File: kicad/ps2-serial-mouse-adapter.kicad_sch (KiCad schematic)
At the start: 12 parts, among them U1 Arduino_Mini, U2 MAX232

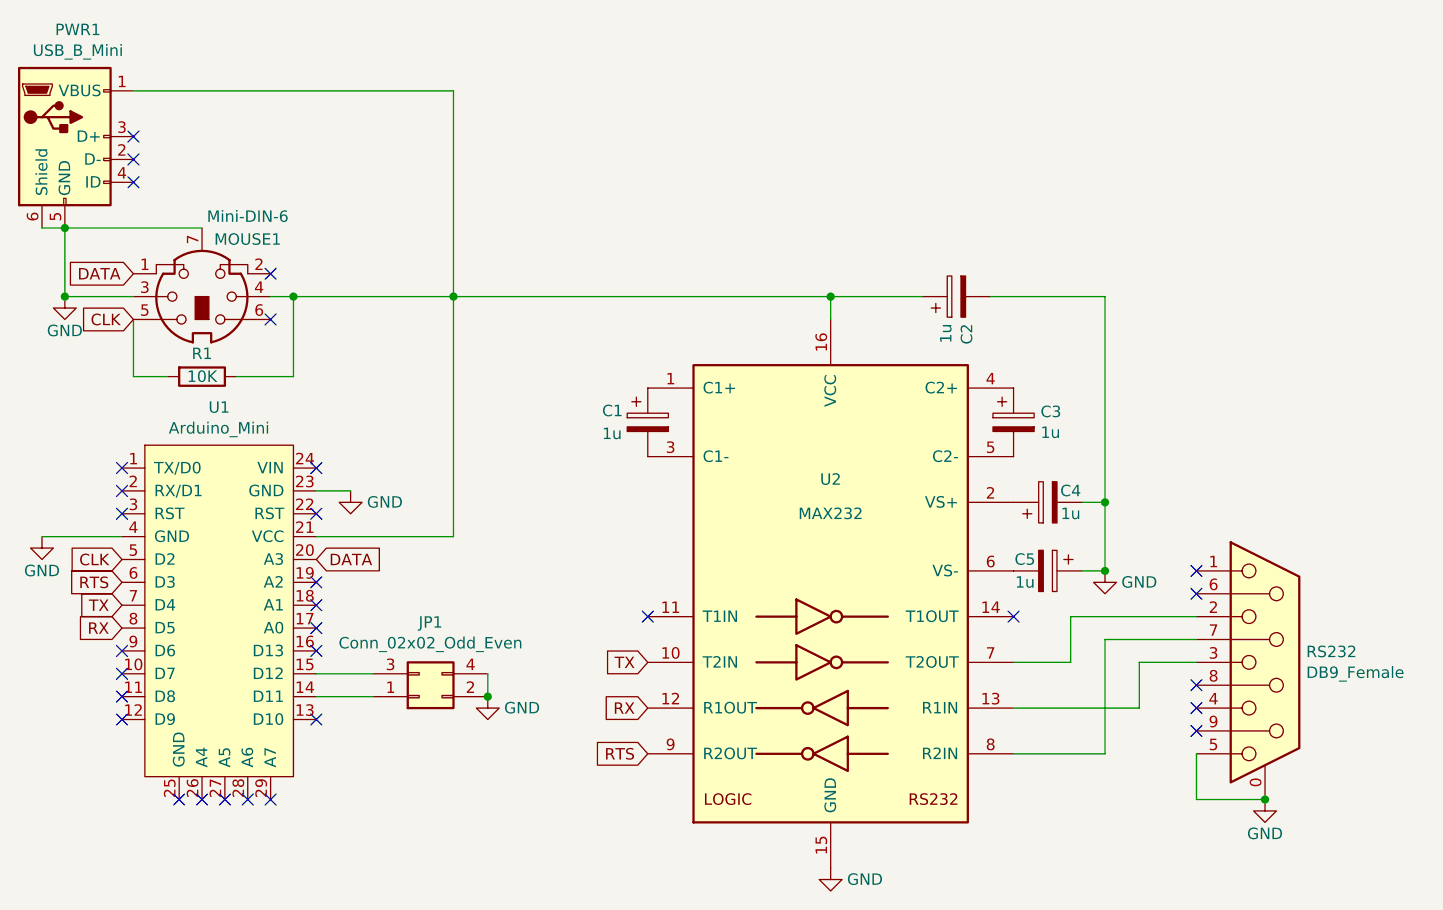
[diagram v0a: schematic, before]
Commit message: Switched charge pump from GND to VCC
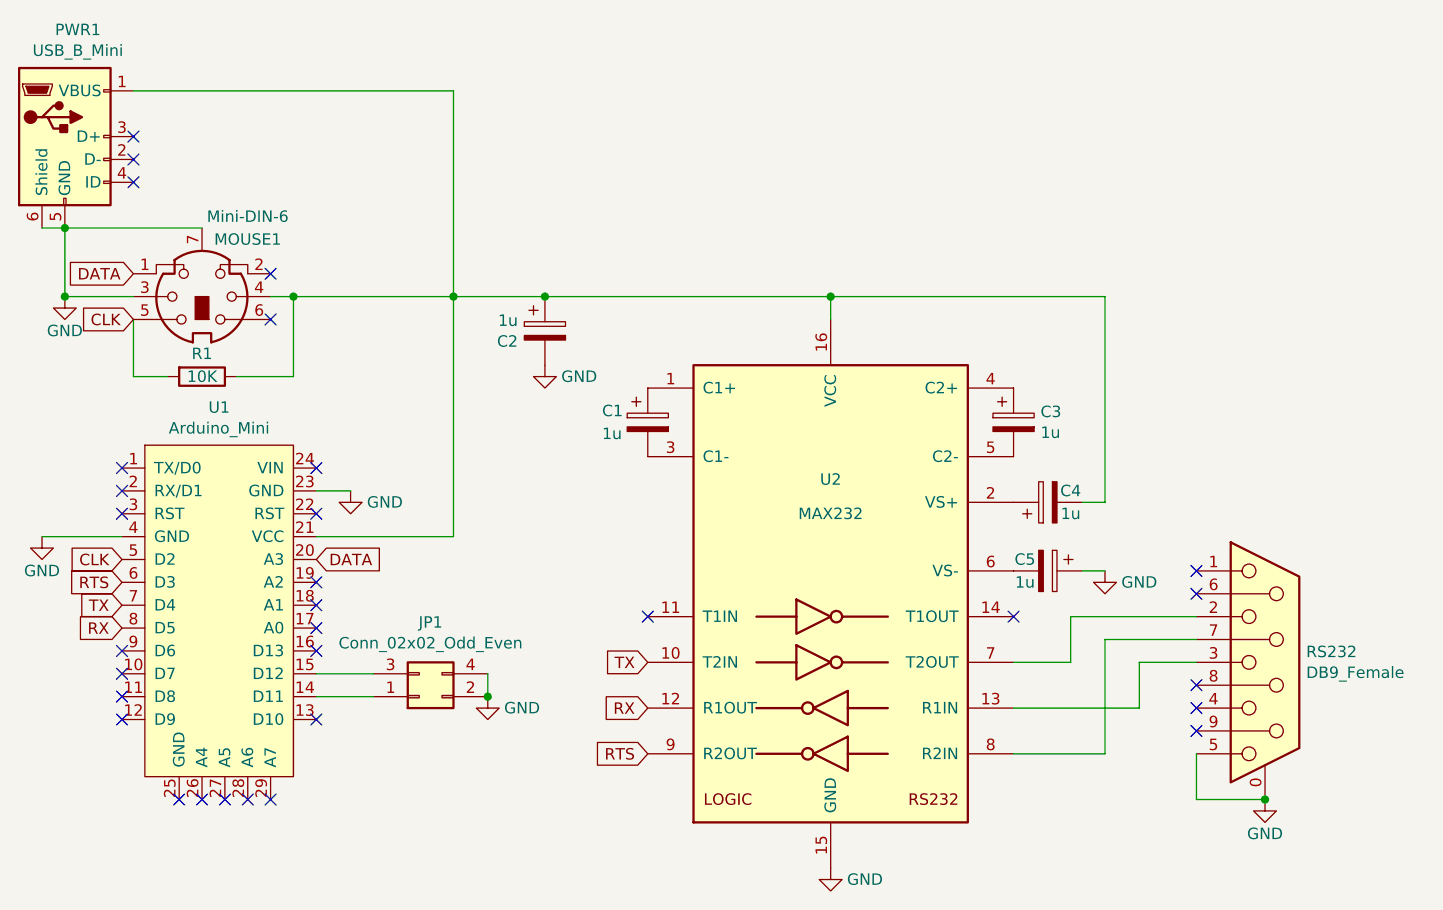
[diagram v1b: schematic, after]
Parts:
- MOUSE1: footprint Necroware:Mini_DIN_6_LCSC_C77848 -> ps2-serial-mouse-adapter:Mini_DIN_6_LCSC_C77848
- PWR1: footprint MyLibrary:USB_Mini-B-Jing_Extension_LSCS_C46398 -> ps2-serial-mouse-adapter:USB_Mini-B-Jing_Extension_LSCS_C46398
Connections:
- net GND: no longer C4.2
- net at C2.1, MOUSE1.4, PWR1.1 (VBUS)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: now also C4.2
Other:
- moved on the sheet: C2
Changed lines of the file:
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@@
   (title_block
     (title "PS/2 to Serial Mouse Adapter")
-    (date "2021-10-22")
-    (rev "0.7")
+    (date "2023-01-22")
+    (rev "0.8")
     (company "Necroware")
     (comment 1 "by Scorp")
@@
   (junction (at 100.33 60.96) (diameter 0) (color 0 0 0 0)
   )
+  (junction (at 160.02 60.96) (diameter 0) (color 0 0 0 0)
+  )
   (junction (at 74.93 60.96) (diameter 0) (color 0 0 0 0)
   )
@@
   (junction (at 118.11 60.96) (diameter 0) (color 0 0 0 0)
   )
-  (junction (at 160.02 60.96) (diameter 0) (color 0 0 0 0)
-  )
   (junction (at 121.92 105.41) (diameter 0) (color 0 0 0 0)
   )
-  (junction (at 190.5 83.82) (diameter 0) (color 0 0 0 0)
-  )
-  (junction (at 190.5 91.44) (diameter 0) (color 0 0 0 0)
+  (junction (at 128.27 60.96) (diameter 0) (color 0 0 0 0)
   )
   (no_connect (at 102.87 97.79))
@@
     (stroke (width 0) (type default) (color 0 0 0 0))
   )
-  (wire (pts (xy 177.8 60.96) (xy 190.5 60.96))
+  (wire (pts (xy 160.02 60.96) (xy 190.5 60.96))
     (stroke (width 0) (type default) (color 0 0 0 0))
   )
@@
     (stroke (width 0) (type default) (color 0 0 0 0))
   )
-  (wire (pts (xy 170.18 60.96) (xy 160.02 60.96))
-    (stroke (width 0) (type default) (color 0 0 0 0))
-  )
   (wire (pts (xy 118.11 87.63) (xy 118.11 60.96))
     (stroke (width 0) (type default) (color 0 0 0 0))
   )
-  (wire (pts (xy 118.11 60.96) (xy 160.02 60.96))
+  (wire (pts (xy 118.11 60.96) (xy 128.27 60.96))
     (stroke (width 0) (type default) (color 0 0 0 0))
   )
@@
     (stroke (width 0) (type default) (color 0 0 0 0))
   )
-  (wire (pts (xy 190.5 83.82) (xy 190.5 91.44))
+  (wire (pts (xy 128.27 60.96) (xy 160.02 60.96))
     (stroke (width 0) (type default) (color 0 0 0 0))
   )
@@
     (property "Reference" "MOUSE1" (id 0) (at 95.25 54.61 0))
     (property "Value" "Mini-DIN-6" (id 1) (at 95.25 52.07 0))
-    (property "Footprint" "Necroware:Mini_DIN_6_LCSC_C77848" (id 2) (at 90.17 60.96 0)
+    (property "Footprint" "ps2-serial-mouse-adapter:Mini_DIN_6_LCSC_C77848" (id 2) (at 90.17 60.96 0)
       (effects (font (size 1.27 1.27)) hide)
     )
@@
     (pin "2")
   )
-  (symbol (lib_id "ps2-serial-mouse-adapter-rescue:CP-Device") (at 173.99 60.96 90) (unit 1)
-    (in_bom yes) (on_board yes)
-    (property "Reference" "C2" (id 0) (at 175.1584 63.9572 0)
+  (symbol (lib_id "ps2-serial-mouse-adapter-rescue:CP-Device") (at 128.27 64.77 0) (unit 1)
+    (in_bom yes) (on_board yes)
+    (property "Reference" "C2" (id 0) (at 125.2728 65.9384 0)
       (effects (font (size 1.27 1.27)) (justify right))
     )
-    (property "Value" "1u" (id 1) (at 172.847 63.9572 0)
+    (property "Value" "1u" (id 1) (at 125.2728 63.627 0)
       (effects (font (size 1.27 1.27)) (justify right))
     )
-    (property "Footprint" "Capacitor_THT:CP_Radial_D4.0mm_P1.50mm" (id 2) (at 177.8 59.9948 0)
-      (effects (font (size 1.27 1.27)) hide)
-    )
-    (property "Datasheet" "~" (id 3) (at 173.99 60.96 0)
+    (property "Footprint" "Capacitor_THT:CP_Radial_D4.0mm_P1.50mm" (id 2) (at 129.2352 68.58 0)
+      (effects (font (size 1.27 1.27)) hide)
+    )
+    (property "Datasheet" "~" (id 3) (at 128.27 64.77 0)
       (effects (font (size 1.27 1.27)) hide)
     )
@@
     (property "Reference" "PWR1" (id 0) (at 76.3778 31.3182 0))
     (property "Value" "USB_B_Mini" (id 1) (at 76.3778 33.6296 0))
-    (property "Footprint" "MyLibrary:USB_Mini-B-Jing_Extension_LSCS_C46398" (id 2) (at 78.74 44.45 0)
+    (property "Footprint" "ps2-serial-mouse-adapter:USB_Mini-B-Jing_Extension_LSCS_C46398" (id 2) (at 78.74 44.45 0)
       (effects (font (size 1.27 1.27)) hide)
     )
@@
     (pin "2")
   )
+  (symbol (lib_id "power:GND") (at 128.27 68.58 0) (unit 1)
+    (in_bom yes) (on_board yes)
+    (property "Reference" "#PWR0101" (id 0) (at 128.27 74.93 0)
+      (effects (font (size 1.27 1.27)) hide)
+    )
+    (property "Value" "GND" (id 1) (at 132.08 69.85 0))
+    (property "Footprint" "" (id 2) (at 128.27 68.58 0)
+      (effects (font (size 1.27 1.27)) hide)
+    )
+    (property "Datasheet" "" (id 3) (at 128.27 68.58 0)
+      (effects (font (size 1.27 1.27)) hide)
+    )
+    (pin "1")
+  )
   (sheet_instances
     (path "/" (page "1"))
@@
       (reference "#PWR07") (unit 1) (value "GND") (footprint "")
     )
+    (path "/ab14643d-1ac0-4d15-b102-1656b995f1d5"
+      (reference "#PWR0101") (unit 1) (value "GND") (footprint "")
+    )
     (path "/00000000-0000-0000-0000-00005fbaa608"
       (reference "C1") (unit 1) (value "1u") (footprint "Capacitor_THT:CP_Radial_D4.0mm_P1.50mm")
@@
     )
     (path "/00000000-0000-0000-0000-00005fba6bf7"
-      (reference "MOUSE1") (unit 1) (value "Mini-DIN-6") (footprint "Necroware:Mini_DIN_6_LCSC_C77848")
+      (reference "MOUSE1") (unit 1) (value "Mini-DIN-6") (footprint "ps2-serial-mouse-adapter:Mini_DIN_6_LCSC_C77848")
     )
     (path "/00000000-0000-0000-0000-00005fbba6cf"
-      (reference "PWR1") (unit 1) (value "USB_B_Mini") (footprint "MyLibrary:USB_Mini-B-Jing_Extension_LSCS_C46398")
+      (reference "PWR1") (unit 1) (value "USB_B_Mini") (footprint "ps2-serial-mouse-adapter:USB_Mini-B-Jing_Extension_LSCS_C46398")
     )
     (path "/00000000-0000-0000-0000-00006172b4af"
